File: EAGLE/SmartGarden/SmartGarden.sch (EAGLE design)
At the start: 8 parts

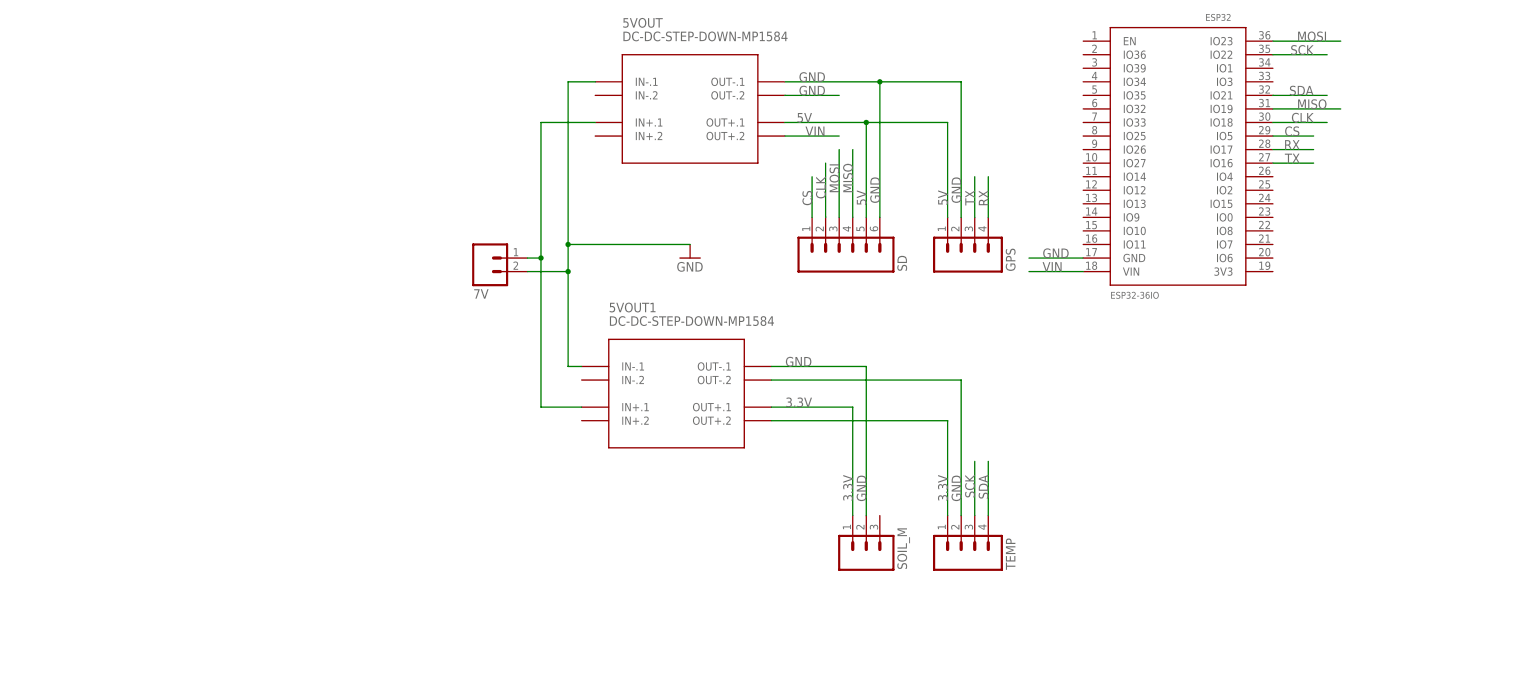
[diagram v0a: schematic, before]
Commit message: Board impress v1 ... problem with the model ESP32
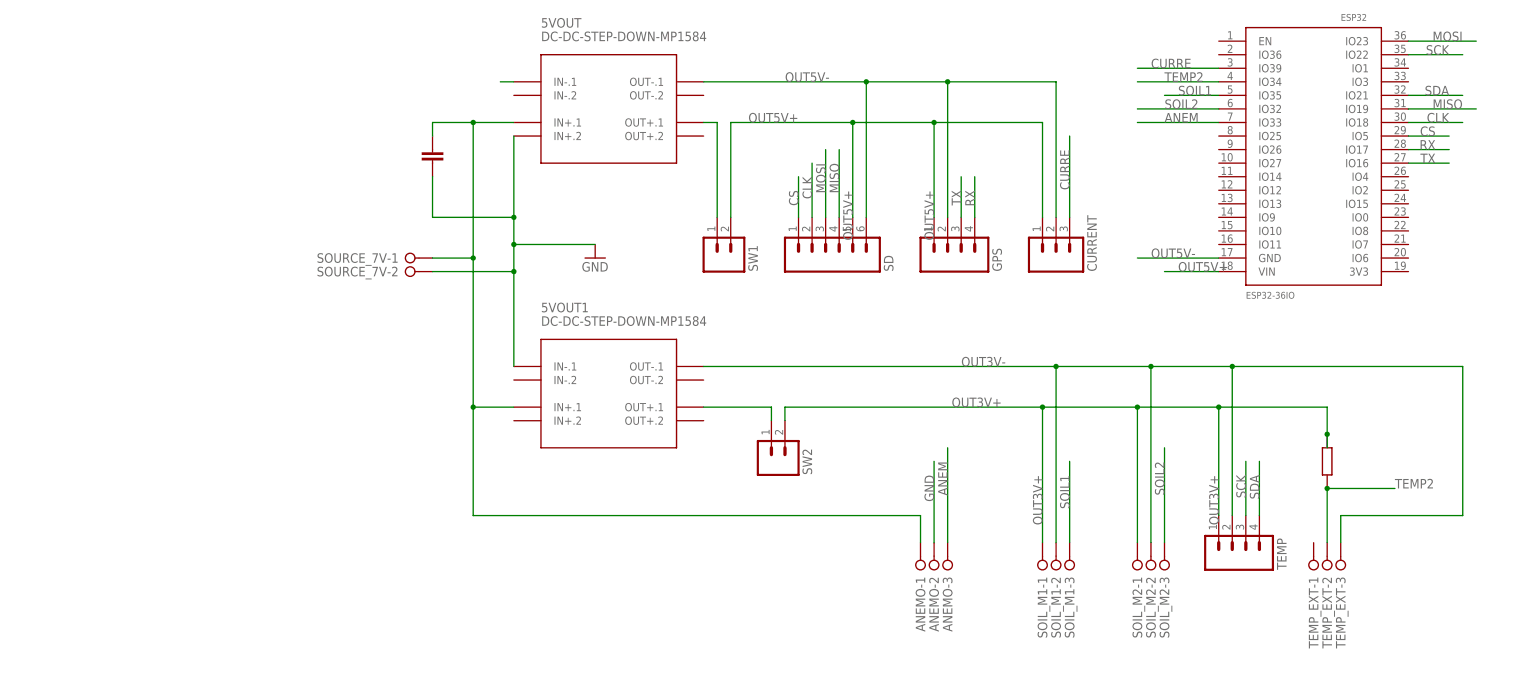
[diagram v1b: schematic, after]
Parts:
- removed 7V: (no value), con-amp-quick:M02
- removed SOIL_M: (no value), con-amp-quick:M03
- added ANEMO, SOIL_M1, SOIL_M2, TEMP_EXT: (no value), con-wago-508:W237-3E
- added C0: (no value), rcl:C-EU025-025X050
- added CURRENT: (no value), con-amp-quick:M03
- added R1: (no value), rcl:R-EU_0204/7
- added SOURCE_7V: (no value), con-wago-508:W237-02P
- added SW1, SW2: (no value), con-amp-quick:M02
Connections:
- removed net 3.3V: 5VOUT1.OUT+.1, 5VOUT1.OUT+.2, SOIL_M.1, TEMP.1
- removed net 5V: 5VOUT.OUT+.1, GPS.1, SD.5
- removed net VIN: 5VOUT.OUT+.2, ESP32.VIN
- new net 7V: 5VOUT.IN+.1, 5VOUT1.IN+.1, ANEMO-1.KL, C0.1, SOURCE_7V-1.KL
- new net ANEM: ANEMO-3.KL, ESP32.IO33
- new net CURRE: CURRENT.3, ESP32.IO39
- new net N$2: 5VOUT1.OUT+.1, SW2.1
- new net N$3: 5VOUT.OUT+.1, SW1.1
- new net OUT3V+: R1.2, SOIL_M1-1.KL, SOIL_M2-1.KL, SW2.2, TEMP.1
- new net OUT3V-: 5VOUT1.OUT-.1, SOIL_M1-2.KL, SOIL_M2-2.KL, TEMP.2, TEMP_EXT-3.KL
- new net OUT5V+: CURRENT.1, ESP32.VIN, GPS.1, SD.5, SW1.2
- new net OUT5V-: 5VOUT.OUT-.1, CURRENT.2, ESP32.GND, GPS.2, SD.6
- new net SOIL1: ESP32.IO35, SOIL_M1-3.KL
- new net SOIL2: ESP32.IO32, SOIL_M2-3.KL
- new net TEMP2: ESP32.IO34, R1.1, TEMP_EXT-2.KL
- net GND: now also 5VOUT.IN+.2, ANEMO-2.KL, C0.2, SOURCE_7V-2.KL; no longer 5VOUT.IN-.1, 5VOUT.OUT-.1, 5VOUT.OUT-.2, 5VOUT1.OUT-.1, 5VOUT1.OUT-.2, 7V.2, ESP32.GND, GPS.2, SD.6, SOIL_M.2, TEMP.2
- net N$1: now also 5VOUT.IN-.1; no longer 5VOUT.IN+.1, 5VOUT1.IN+.1, 7V.1
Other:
- moved on the sheet: 5VOUT, 5VOUT1, ESP32, GPS, SD, TEMP

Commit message: Update eagle
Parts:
- removed 5VOUT1: DC-DC-STEP-DOWN-MP1584, diy-modules:DC-DC-STEP-DOWN-MP1584
- removed C0: (no value), rcl:C-EU025-025X050
- added 3V3OUT: DC-DC-STEP-DOWN-MP1584, diy-modules:DC-DC-STEP-DOWN-MP1584
- added C3V, C5V, C7V: (no value), rcl:C-EU025-025X050
- ESP32: value ESP32-36IO -> ESP32DEVKITC; device ESP32:ESP32-36IO -> ESP32:ESP32DEVKITC
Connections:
- net RX renamed RX_GPS
- net TX renamed TX_GPS
- removed net CURRE: CURRENT.3, ESP32.IO39
- removed net N$1: 5VOUT.IN-.1
- removed net OUT3V-: 5VOUT1.OUT-.1, SOIL_M1-2.KL, SOIL_M2-2.KL, TEMP.2, TEMP_EXT-3.KL
- removed net OUT5V-: 5VOUT.OUT-.1, CURRENT.2, ESP32.GND, GPS.2, SD.6
- new net CURRENT: CURRENT.3, ESP32.IO4
- net 7V: now also 3V3OUT.IN+.1, C7V.1; no longer 5VOUT1.IN+.1, C0.1
- net ANEM: now also ESP32.IO32; no longer ESP32.IO33
- net CLK: now also ESP32.SCK; no longer ESP32.IO18
- net GND: now also 3V3OUT.IN-.1, 3V3OUT.OUT-.1, 5VOUT.IN-.1, 5VOUT.OUT-.1, C3V.1, C5V.1, C7V.2, CURRENT.2, ESP32.GND@14, GPS.2, SD.6, SOIL_M1-2.KL, SOIL_M2-2.KL, TEMP.2, TEMP_EXT-3.KL; no longer 5VOUT.IN+.2, 5VOUT1.IN-.1, C0.2
- net N$2: now also 3V3OUT.OUT+.1, C3V.2; no longer 5VOUT1.OUT+.1
- net N$3: now also C5V.2
- net OUT5V+: now also ESP32.5V; no longer ESP32.VIN
- net SCK: now also ESP32.SCL; no longer ESP32.IO22
- net SDA: now also ESP32.SDA; no longer ESP32.IO21
- net SOIL1: now also ESP32.BATS; no longer ESP32.IO35
- net SOIL2: now also ESP32.TARE; no longer ESP32.IO32
- net TEMP2: now also ESP32.BAT_BOT; no longer ESP32.IO34
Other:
- moved on the sheet: 5VOUT, SOURCE_7V-1, SOURCE_7V-2, TEMP
